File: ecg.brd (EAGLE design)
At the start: 56 x 85 mm, 21 parts, among them IC1 ADP151, U1 TMP102AIDRLT, U2 TMP102AIDRLT, U3 ADAS1000BSTZ

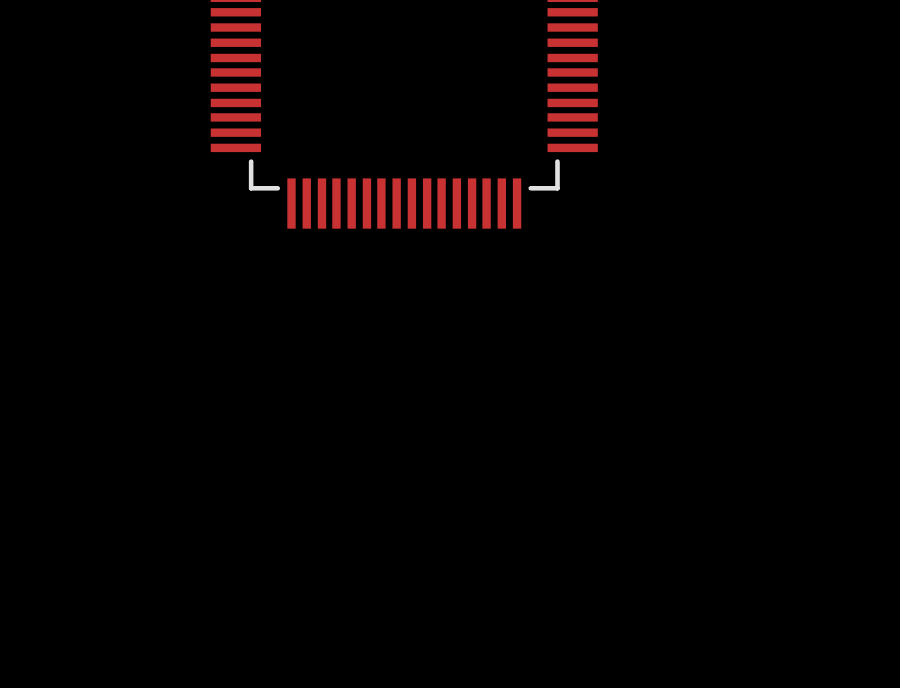
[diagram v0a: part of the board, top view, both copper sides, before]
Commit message: Added XTAL
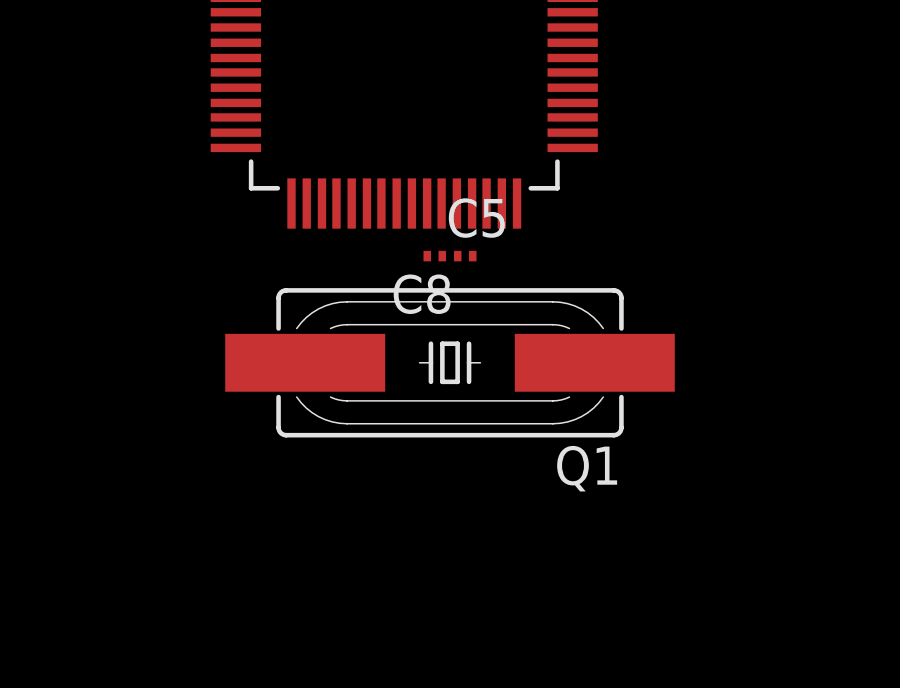
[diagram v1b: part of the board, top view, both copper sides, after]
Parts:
- added C5, C8: (no value), rcl:C0201
- added Q1: (no value), crystal:HC49UP
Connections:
- new net N$3: LED2.A, R4.1
- new net N$6: C5.1, Q1.1, U3.28
- net +3V3: now also R5.2, R7.2; no longer LED1.A, LED3.A
- net +5V: now also R4.2; no longer LED2.A
- net GND: now also C5.2, C8.2, LED1.C, LED2.C, LED3.C; no longer R4.1, R5.1, R7.1
- net N$2: now also LED1.A, R5.1; no longer LED1.C, R5.2
- net N$5: now also LED3.A, R7.1; no longer LED2.C, R4.2
- net N$7: now also C8.1, Q1.2, U3.27; no longer LED3.C, R7.2
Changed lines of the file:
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@@
 <element name="C7" library="resistor" package="C0805K" value="10uF cer" x="0.762" y="-9.398"/>
 <element name="C4" library="resistor" package="C0805K" value="10uF cer" x="0.762" y="-14.224"/>
+<element name="Q1" library="crystal" package="HC49UP" value="" x="24.13" y="54.102" rot="R180">
+<attribute name="OC_NEWARK" value="unknown" x="24.13" y="54.102" size="1.778" layer="27" rot="R180" display="off"/>
+<attribute name="MPN" value="" x="24.13" y="54.102" size="1.778" layer="27" rot="R180" display="off"/>
+<attribute name="MF" value="" x="24.13" y="54.102" size="1.778" layer="27" rot="R180" display="off"/>
+<attribute name="OC_FARNELL" value="unknown" x="24.13" y="54.102" size="1.778" layer="27" rot="R180" display="off"/>
+</element>
+<element name="C5" library="rcl" package="C0201" value="" x="24.638" y="57.658"/>
+<element name="C8" library="rcl" package="C0201" value="" x="23.622" y="57.658" rot="R180"/>
 </elements>
 <signals>
@@
 <contactref element="C3" pad="2"/>
 <contactref element="U1" pad="2"/>
-<contactref element="R5" pad="1"/>
 <contactref element="IC1" pad="2"/>
 <contactref element="IC1" pad="2"/>
 <contactref element="C6" pad="2"/>
-<contactref element="R4" pad="1"/>
-<contactref element="R7" pad="1"/>
 <contactref element="C7" pad="2"/>
 <contactref element="C4" pad="2"/>
+<contactref element="LED1" pad="C"/>
+<contactref element="LED2" pad="C"/>
+<contactref element="LED3" pad="C"/>
+<contactref element="C8" pad="2"/>
+<contactref element="C5" pad="2"/>
 <wire x1="41.402" y1="77.448" x2="53.848" y2="77.47" width="0" layer="19" extent="1-1"/>
 <wire x1="36.2966" y1="73.66" x2="41.402" y2="77.448" width="0" layer="19" extent="1-1"/>
 <wire x1="34.8234" y1="74.168" x2="36.2966" y2="73.66" width="0" layer="19" extent="1-1"/>
-<wire x1="32.004" y1="75.096" x2="34.8234" y2="74.168" width="0" layer="19" extent="1-1"/>
-<wire x1="34.71" y1="80.772" x2="32.004" y2="75.096" width="0" layer="19" extent="1-1"/>
-<wire x1="6.008" y1="50.038" x2="32.004" y2="75.096" width="0" layer="19" extent="1-1"/>
+<wire x1="32.004" y1="79.514" x2="34.8234" y2="74.168" width="0" layer="19" extent="1-1"/>
+<wire x1="34.71" y1="80.772" x2="32.004" y2="79.514" width="0" layer="19" extent="1-1"/>
+<wire x1="24.888" y1="57.658" x2="34.8234" y2="74.168" width="0" layer="19" extent="1-1"/>
+<wire x1="23.372" y1="57.658" x2="24.888" y2="57.658" width="0" layer="19" extent="1-1"/>
+<wire x1="6.008" y1="50.038" x2="23.372" y2="57.658" width="0" layer="19" extent="1-1"/>
 <wire x1="6.1214" y1="43.434" x2="6.008" y2="50.038" width="0" layer="19" extent="1-1"/>
 <wire x1="19.138" y1="31.75" x2="6.1214" y2="43.434" width="0" layer="19" extent="1-1"/>
-<wire x1="17.438" y1="22.606" x2="19.138" y2="31.75" width="0" layer="19" extent="1-1"/>
-<wire x1="17.438" y1="13.462" x2="17.438" y2="22.606" width="0" layer="19" extent="1-1"/>
+<wire x1="17.538" y1="26.416" x2="19.138" y2="31.75" width="0" layer="19" extent="1-1"/>
+<wire x1="17.538" y1="17.272" x2="17.538" y2="26.416" width="0" layer="19" extent="1-1"/>
 <wire x1="27.686" y1="36.5459" x2="19.138" y2="31.75" width="0" layer="19" extent="1-1"/>
-<wire x1="1.762" y1="-9.398" x2="17.438" y2="13.462" width="0" layer="19" extent="1-1"/>
+<wire x1="1.762" y1="-9.398" x2="17.538" y2="17.272" width="0" layer="19" extent="1-1"/>
 <wire x1="1.762" y1="-14.224" x2="1.762" y2="-9.398" width="0" layer="19" extent="1-1"/>
 </signal>
@@
 <contactref element="C2" pad="+"/>
 <contactref element="C3" pad="1"/>
-<contactref element="LED1" pad="A"/>
 <contactref element="IC1" pad="5"/>
 <contactref element="C6" pad="1"/>
-<contactref element="LED3" pad="A"/>
 <contactref element="C4" pad="1"/>
+<contactref element="R5" pad="2"/>
+<contactref element="R7" pad="2"/>
 <wire x1="41.402" y1="81.048" x2="51.308" y2="82.55" width="0" layer="19" extent="1-1"/>
 <wire x1="36.41" y1="80.772" x2="41.402" y2="81.048" width="0" layer="19" extent="1-1"/>
-<wire x1="32.004" y1="81.014" x2="36.41" y2="80.772" width="0" layer="19" extent="1-1"/>
-<wire x1="36.2966" y1="74.168" x2="36.41" y2="80.772" width="0" layer="19" extent="1-1"/>
+<wire x1="32.004" y1="76.796" x2="36.41" y2="80.772" width="0" layer="19" extent="1-1"/>
+<wire x1="36.2966" y1="74.168" x2="32.004" y2="76.796" width="0" layer="19" extent="1-1"/>
 <wire x1="36.41" y1="70.612" x2="36.2966" y2="74.168" width="0" layer="19" extent="1-1"/>
 <wire x1="39.624" y1="71.032" x2="36.41" y2="70.612" width="0" layer="19" extent="1-1"/>
@@
 <wire x1="7.5946" y1="43.434" x2="7.5946" y2="42.926" width="0" layer="19" extent="1-1"/>
 <wire x1="7.708" y1="50.038" x2="7.5946" y2="43.434" width="0" layer="19" extent="1-1"/>
-<wire x1="19.038" y1="17.272" x2="17.438" y2="31.75" width="0" layer="19" extent="1-1"/>
-<wire x1="-0.238" y1="-14.224" x2="19.038" y2="17.272" width="0" layer="19" extent="1-1"/>
-</signal>
-<signal name="N$2">
-<contactref element="R5" pad="2"/>
-<contactref element="LED1" pad="C"/>
-<wire x1="32.004" y1="76.796" x2="32.004" y2="79.514" width="0" layer="19" extent="1-1"/>
+<wire x1="19.138" y1="13.462" x2="17.438" y2="31.75" width="0" layer="19" extent="1-1"/>
+<wire x1="-0.238" y1="-14.224" x2="19.138" y2="13.462" width="0" layer="19" extent="1-1"/>
 </signal>
 <signal name="+5V">
@@
 <contactref element="IC1" pad="3"/>
 <contactref element="IC1" pad="1"/>
-<contactref element="LED2" pad="A"/>
 <contactref element="C7" pad="1"/>
+<contactref element="R4" pad="2"/>
 <wire x1="28.636" y1="36.5459" x2="53.848" y2="82.55" width="0" layer="19" extent="1-1"/>
 <wire x1="26.736" y1="36.5459" x2="28.636" y2="36.5459" width="0" layer="19" extent="1-1"/>
-<wire x1="19.038" y1="26.416" x2="26.736" y2="36.5459" width="0" layer="19" extent="1-1"/>
-<wire x1="-0.238" y1="-9.398" x2="19.038" y2="26.416" width="0" layer="19" extent="1-1"/>
+<wire x1="19.138" y1="22.606" x2="26.736" y2="36.5459" width="0" layer="19" extent="1-1"/>
+<wire x1="-0.238" y1="-9.398" x2="19.138" y2="22.606" width="0" layer="19" extent="1-1"/>
+</signal>
+<signal name="N$2">
+<contactref element="R5" pad="1"/>
+<contactref element="LED1" pad="A"/>
+<wire x1="32.004" y1="75.096" x2="32.004" y2="81.014" width="0" layer="19" extent="1-1"/>
+</signal>
+<signal name="N$3">
+<contactref element="R4" pad="1"/>
+<contactref element="LED2" pad="A"/>
+<wire x1="17.438" y1="22.606" x2="19.038" y2="26.416" width="0" layer="19" extent="1-1"/>
 </signal>
 <signal name="N$5">
-<contactref element="LED2" pad="C"/>
-<contactref element="R4" pad="2"/>
-<wire x1="17.538" y1="26.416" x2="19.138" y2="22.606" width="0" layer="19" extent="1-1"/>
+<contactref element="R7" pad="1"/>
+<contactref element="LED3" pad="A"/>
+<wire x1="17.438" y1="13.462" x2="19.038" y2="17.272" width="0" layer="19" extent="1-1"/>
 </signal>
 <signal name="N$7">
-<contactref element="LED3" pad="C"/>
-<contactref element="R7" pad="2"/>
-<wire x1="17.538" y1="17.272" x2="19.138" y2="13.462" width="0" layer="19" extent="1-1"/>
+<contactref element="U3" pad="27"/>
+<contactref element="Q1" pad="2"/>
+<contactref element="C8" pad="1"/>
+<wire x1="19.304" y1="54.102" x2="23.872" y2="57.658" width="0" layer="19" extent="1-1"/>
+<wire x1="23.872" y1="57.658" x2="23.8506" y2="59.4106" width="0" layer="19" extent="1-1"/>
+</signal>
+<signal name="N$6">
+<contactref element="U3" pad="28"/>
+<contactref element="Q1" pad="1"/>
+<contactref element="C5" pad="1"/>
+<wire x1="28.956" y1="54.102" x2="24.388" y2="57.658" width="0" layer="19" extent="1-1"/>
+<wire x1="24.388" y1="57.658" x2="24.3586" y2="59.4106" width="0" layer="19" extent="1-1"/>
 </signal>
 </signals>

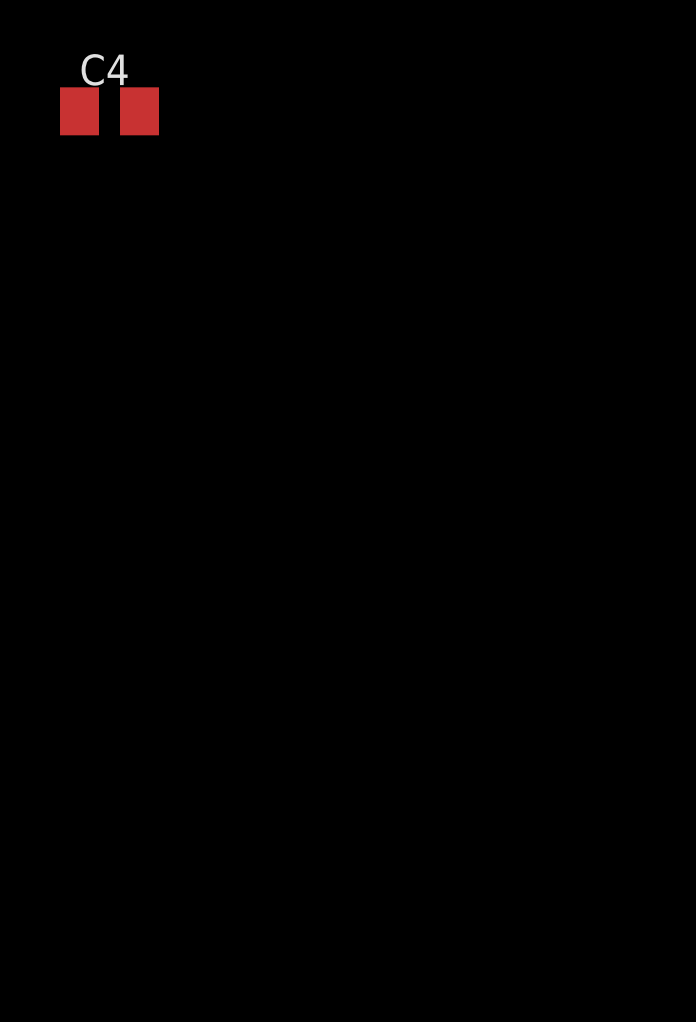
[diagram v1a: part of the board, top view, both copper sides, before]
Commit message: Added second voltage regulator for digital domain. Changed the frame to a bigger one.
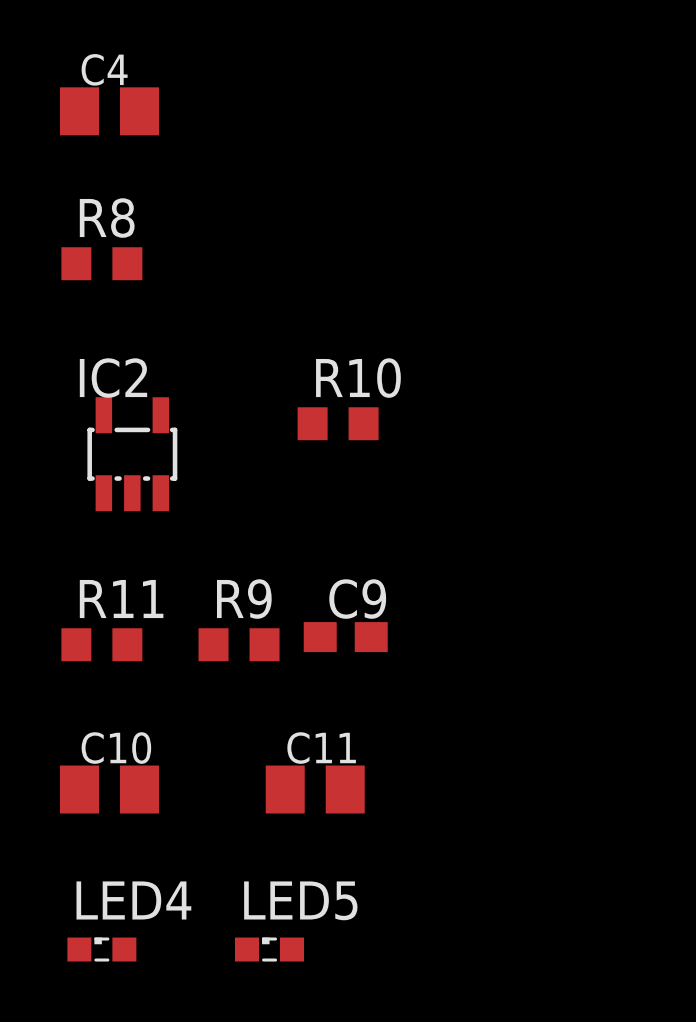
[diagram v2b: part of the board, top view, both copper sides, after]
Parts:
- added C10, C11: 10uF cer, resistor:C0805K
- added C9: 100n, eagle-ltspice:C0603
- added IC2: ADP151, v-reg-micrel:SOT23-5
- added LED4, LED5: (no value), eagle-ltspice:LED_SML0603
- added R10, R9: 1k, resistor:R0603
- added R11, R8: 10k, resistor:R0603
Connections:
- new net +3V3ADCVDD: C4.1, C6.1, IC1.5, R7.2
- new net +3V3IOVDD: C11.1, C9.1, IC2.5, R10.2
- new net N$10: LED5.A, R10.1
- new net N$11: IC2.3, R11.1
- new net N$8: IC1.3, R8.1
- new net N$9: LED4.A, R9.1
- net +3V3: no longer C4.1, C6.1, IC1.5, R7.2
- net +5V: now also C10.1, IC2.1, R11.2, R8.2, R9.2; no longer IC1.3
- net GND: now also C10.2, C11.2, C9.2, IC2.2, LED4.C, LED5.C
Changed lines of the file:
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@@
 <element name="C5" library="rcl" package="C0201" value="" x="24.638" y="57.658"/>
 <element name="C8" library="rcl" package="C0201" value="" x="23.622" y="57.658" rot="R180"/>
+<element name="R8" library="resistor" package="R0603" value="10k" x="0.508" y="-19.304"/>
+<element name="IC2" library="v-reg-micrel" package="SOT23-5" value="ADP151" x="1.524" y="-25.654">
+<attribute name="OC_NEWARK" value="09J8939" x="1.524" y="-25.654" size="1.778" layer="27" display="off"/>
+<attribute name="MPN" value="MIC5219BM5 TR" x="1.524" y="-25.654" size="1.778" layer="27" display="off"/>
+<attribute name="MF" value="ALTERA CORPORATION" x="1.524" y="-25.654" size="1.778" layer="27" display="off"/>
+<attribute name="OC_FARNELL" value="1100656" x="1.524" y="-25.654" size="1.778" layer="27" display="off"/>
+</element>
+<element name="C9" library="eagle-ltspice" package="C0603" value="100n" x="8.636" y="-31.75">
+<attribute name="SPICEMODEL" value="NONE" x="0.508" y="-31.75" size="1.778" layer="27" display="off"/>
+<attribute name="SPICEPREFIX" value="C" x="0.508" y="-31.75" size="1.778" layer="27" display="off"/>
+</element>
+<element name="LED4" library="eagle-ltspice" package="LED_SML0603" value="" x="0.508" y="-42.164">
+<attribute name="SPICEMODEL" value="NONE" x="0.508" y="-37.084" size="1.778" layer="27" display="off"/>
+<attribute name="SPICETYPE" value="diode" x="0.508" y="-37.084" size="1.778" layer="27" display="off"/>
+<attribute name="SPICEPREFIX" value="D" x="0.508" y="-37.084" size="1.778" layer="27" display="off"/>
+</element>
+<element name="R9" library="resistor" package="R0603" value="1k" x="5.08" y="-32.004"/>
+<element name="LED5" library="eagle-ltspice" package="LED_SML0603" value="" x="6.096" y="-42.164">
+<attribute name="SPICEMODEL" value="NONE" x="0.508" y="-46.228" size="1.778" layer="27" display="off"/>
+<attribute name="SPICETYPE" value="diode" x="0.508" y="-46.228" size="1.778" layer="27" display="off"/>
+<attribute name="SPICEPREFIX" value="D" x="0.508" y="-46.228" size="1.778" layer="27" display="off"/>
+</element>
+<element name="R10" library="resistor" package="R0603" value="1k" x="8.382" y="-24.638"/>
+<element name="C10" library="resistor" package="C0805K" value="10uF cer" x="0.762" y="-36.83"/>
+<element name="C11" library="resistor" package="C0805K" value="10uF cer" x="7.62" y="-36.83"/>
+<element name="R11" library="resistor" package="R0603" value="10k" x="0.508" y="-32.004"/>
 </elements>
 <signals>
@@
 <contactref element="C8" pad="2"/>
 <contactref element="C5" pad="2"/>
+<contactref element="IC2" pad="2"/>
+<contactref element="IC2" pad="2"/>
+<contactref element="C9" pad="2"/>
+<contactref element="C10" pad="2"/>
+<contactref element="C11" pad="2"/>
+<contactref element="LED4" pad="C"/>
+<contactref element="LED5" pad="C"/>
 <wire x1="41.402" y1="77.448" x2="53.848" y2="77.47" width="0" layer="19" extent="1-1"/>
 <wire x1="36.2966" y1="73.66" x2="41.402" y2="77.448" width="0" layer="19" extent="1-1"/>
@@
 <wire x1="1.762" y1="-9.398" x2="17.538" y2="17.272" width="0" layer="19" extent="1-1"/>
 <wire x1="1.762" y1="-14.224" x2="1.762" y2="-9.398" width="0" layer="19" extent="1-1"/>
+<wire x1="1.524" y1="-26.9541" x2="1.762" y2="-14.224" width="0" layer="19" extent="1-1"/>
+<wire x1="9.486" y1="-31.75" x2="1.524" y2="-26.9541" width="0" layer="19" extent="1-1"/>
+<wire x1="8.62" y1="-36.83" x2="9.486" y2="-31.75" width="0" layer="19" extent="1-1"/>
+<wire x1="5.346" y1="-42.164" x2="8.62" y2="-36.83" width="0" layer="19" extent="1-1"/>
+<wire x1="-0.242" y1="-42.164" x2="5.346" y2="-42.164" width="0" layer="19" extent="1-1"/>
+<wire x1="1.762" y1="-36.83" x2="-0.242" y2="-42.164" width="0" layer="19" extent="1-1"/>
 </signal>
 <signal name="SDA">
@@
 <contactref element="C2" pad="+"/>
 <contactref element="C3" pad="1"/>
-<contactref element="IC1" pad="5"/>
-<contactref element="C6" pad="1"/>
-<contactref element="C4" pad="1"/>
 <contactref element="R5" pad="2"/>
-<contactref element="R7" pad="2"/>
 <wire x1="41.402" y1="81.048" x2="51.308" y2="82.55" width="0" layer="19" extent="1-1"/>
 <wire x1="36.41" y1="80.772" x2="41.402" y2="81.048" width="0" layer="19" extent="1-1"/>
@@
 <wire x1="39.624" y1="71.032" x2="36.41" y2="70.612" width="0" layer="19" extent="1-1"/>
 <wire x1="39.712" y1="68.072" x2="39.624" y2="71.032" width="0" layer="19" extent="1-1"/>
-<wire x1="26.736" y1="39.1461" x2="39.712" y2="68.072" width="0" layer="19" extent="1-1"/>
-<wire x1="17.438" y1="31.75" x2="26.736" y2="39.1461" width="0" layer="19" extent="1-1"/>
-<wire x1="7.962" y1="39.878" x2="17.438" y2="31.75" width="0" layer="19" extent="1-1"/>
-<wire x1="7.5946" y1="42.926" x2="7.962" y2="39.878" width="0" layer="19" extent="1-1"/>
-<wire x1="7.5946" y1="43.434" x2="7.5946" y2="42.926" width="0" layer="19" extent="1-1"/>
-<wire x1="7.708" y1="50.038" x2="7.5946" y2="43.434" width="0" layer="19" extent="1-1"/>
-<wire x1="19.138" y1="13.462" x2="17.438" y2="31.75" width="0" layer="19" extent="1-1"/>
-<wire x1="-0.238" y1="-14.224" x2="19.138" y2="13.462" width="0" layer="19" extent="1-1"/>
+<wire x1="7.708" y1="50.038" x2="36.41" y2="70.612" width="0" layer="19" extent="1-1"/>
+<wire x1="7.5946" y1="43.434" x2="7.708" y2="50.038" width="0" layer="19" extent="1-1"/>
+<wire x1="7.5946" y1="42.926" x2="7.5946" y2="43.434" width="0" layer="19" extent="1-1"/>
+<wire x1="7.962" y1="39.878" x2="7.5946" y2="42.926" width="0" layer="19" extent="1-1"/>
 </signal>
 <signal name="+5V">
 <contactref element="RPI" pad="2"/>
-<contactref element="IC1" pad="3"/>
 <contactref element="IC1" pad="1"/>
 <contactref element="C7" pad="1"/>
 <contactref element="R4" pad="2"/>
-<wire x1="28.636" y1="36.5459" x2="53.848" y2="82.55" width="0" layer="19" extent="1-1"/>
-<wire x1="26.736" y1="36.5459" x2="28.636" y2="36.5459" width="0" layer="19" extent="1-1"/>
+<contactref element="R8" pad="2"/>
+<contactref element="IC2" pad="1"/>
+<contactref element="C10" pad="1"/>
+<contactref element="R9" pad="2"/>
+<contactref element="R11" pad="2"/>
+<wire x1="26.736" y1="36.5459" x2="53.848" y2="82.55" width="0" layer="19" extent="1-1"/>
 <wire x1="19.138" y1="22.606" x2="26.736" y2="36.5459" width="0" layer="19" extent="1-1"/>
 <wire x1="-0.238" y1="-9.398" x2="19.138" y2="22.606" width="0" layer="19" extent="1-1"/>
+<wire x1="1.358" y1="-19.304" x2="-0.238" y2="-9.398" width="0" layer="19" extent="1-1"/>
+<wire x1="0.574" y1="-26.9541" x2="1.358" y2="-19.304" width="0" layer="19" extent="1-1"/>
+<wire x1="1.358" y1="-32.004" x2="0.574" y2="-26.9541" width="0" layer="19" extent="1-1"/>
+<wire x1="5.93" y1="-32.004" x2="1.358" y2="-32.004" width="0" layer="19" extent="1-1"/>
+<wire x1="-0.238" y1="-36.83" x2="1.358" y2="-32.004" width="0" layer="19" extent="1-1"/>
 </signal>
 <signal name="N$2">
@@
 <wire x1="24.388" y1="57.658" x2="24.3586" y2="59.4106" width="0" layer="19" extent="1-1"/>
 </signal>
+<signal name="N$8">
+<contactref element="R8" pad="1"/>
+<contactref element="IC1" pad="3"/>
+<wire x1="-0.342" y1="-19.304" x2="28.636" y2="36.5459" width="0" layer="19" extent="1-1"/>
+</signal>
+<signal name="N$9">
+<contactref element="R9" pad="1"/>
+<contactref element="LED4" pad="A"/>
+<wire x1="4.23" y1="-32.004" x2="1.258" y2="-42.164" width="0" layer="19" extent="1-1"/>
+</signal>
+<signal name="N$10">
+<contactref element="R10" pad="1"/>
+<contactref element="LED5" pad="A"/>
+<wire x1="7.532" y1="-24.638" x2="6.846" y2="-42.164" width="0" layer="19" extent="1-1"/>
+</signal>
+<signal name="N$11">
+<contactref element="R11" pad="1"/>
+<contactref element="IC2" pad="3"/>
+<wire x1="2.474" y1="-26.9541" x2="-0.342" y2="-32.004" width="0" layer="19" extent="1-1"/>
+</signal>
+<signal name="+3V3ADCVDD">
+<contactref element="IC1" pad="5"/>
+<contactref element="C6" pad="1"/>
+<contactref element="C4" pad="1"/>
+<contactref element="R7" pad="2"/>
+<wire x1="17.438" y1="31.75" x2="26.736" y2="39.1461" width="0" layer="19" extent="1-1"/>
+<wire x1="19.138" y1="13.462" x2="17.438" y2="31.75" width="0" layer="19" extent="1-1"/>
+<wire x1="-0.238" y1="-14.224" x2="19.138" y2="13.462" width="0" layer="19" extent="1-1"/>
+</signal>
+<signal name="+3V3IOVDD">
+<contactref element="IC2" pad="5"/>
+<contactref element="C9" pad="1"/>
+<contactref element="C11" pad="1"/>
+<contactref element="R10" pad="2"/>
+<wire x1="7.786" y1="-31.75" x2="6.62" y2="-36.83" width="0" layer="19" extent="1-1"/>
+<wire x1="9.232" y1="-24.638" x2="7.786" y2="-31.75" width="0" layer="19" extent="1-1"/>
+<wire x1="0.574" y1="-24.3539" x2="9.232" y2="-24.638" width="0" layer="19" extent="1-1"/>
+</signal>
 </signals>
